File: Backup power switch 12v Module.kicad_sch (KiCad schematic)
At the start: 23 parts, among them J2 External, J5 Esternal, J9 PWR SELECTOR, K1 SRD-12VDC-SL-C, Q3 BSS138, U7 ESP32-C3 Pro Mini, U8 AMS1117-3.3

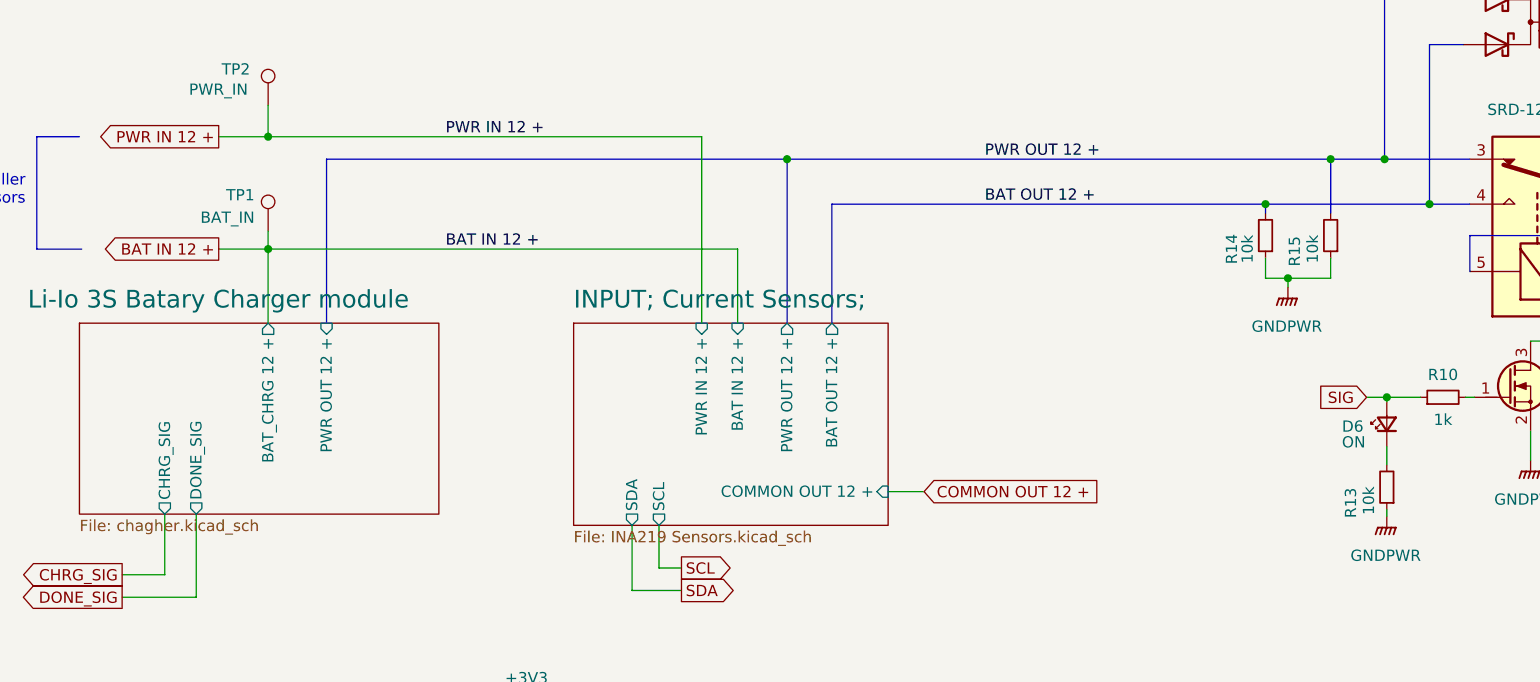
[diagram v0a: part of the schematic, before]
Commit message: Fix charger in/out nammes
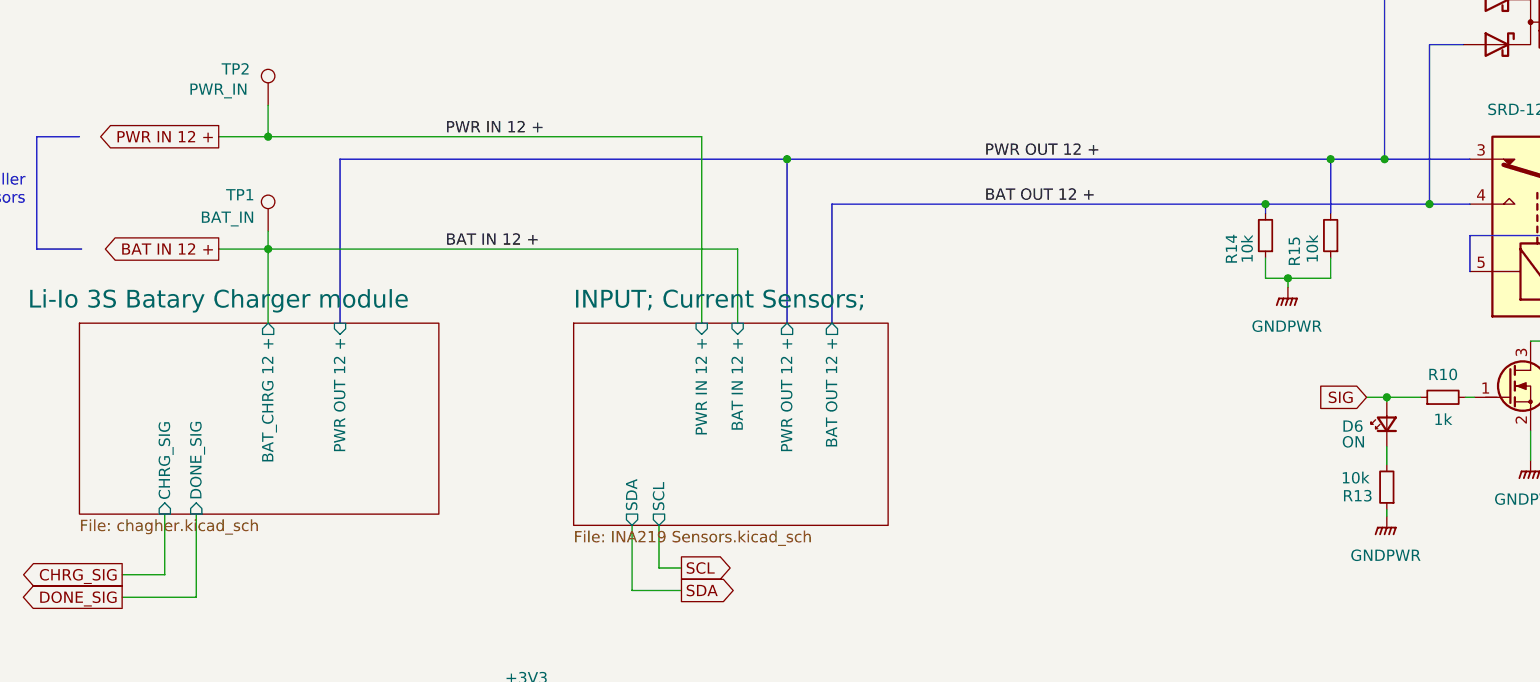
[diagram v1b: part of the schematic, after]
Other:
- sheet INPUT; Current Sensors; ports: added none; removed COMMON OUT 12 +
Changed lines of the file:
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@@
 	(bus
 		(pts
-			(xy 69.342 57.404) (xy 121.412 57.404)
+			(xy 70.866 57.404) (xy 121.412 57.404)
 		)
 		(stroke
@@
 	(wire
 		(pts
-			(xy 132.842 94.996) (xy 136.906 94.996)
-		)
-		(stroke
-			(width 0)
-			(type default)
-		)
-	)
-	(wire
-		(pts
 			(xy 213.868 77.978) (xy 214.376 77.978)
 		)
@@
 	(bus
 		(pts
-			(xy 69.342 57.404) (xy 69.342 75.946)
+			(xy 70.866 57.404) (xy 70.866 75.946)
 		)
 		(stroke
@@
 		)
 	)
-	(global_label "COMMON OUT 12 +"
-		(shape input)
-		(at 136.906 94.996 0)
-		(fields_autoplaced yes)
-		(effects
-			(font
-				(size 1.27 1.27)
-			)
-			(justify left)
-		)
-		(property "Intersheetrefs" "${INTERSHEET_REFS}"
-			(at 158.5783 94.996 0)
-			(show_name yes)
-			(effects
-				(font
-					(size 1.27 1.27)
-				)
-				(justify left)
-				(hide yes)
-			)
-		)
-	)
 	(global_label "BAT IN 12 +"
 		(shape input)
@@
 		(dnp no)
 		(property "Reference" "R13"
-			(at 185.166 96.266 90)
+			(at 185.928 95.504 0)
 			(effects
 				(font
@@
 		)
 		(property "Value" "10k"
-			(at 187.198 96.012 90)
+			(at 185.674 93.472 0)
 			(effects
 				(font
@@
 			)
 		)
-		(pin "COMMON OUT 12 +" input
-			(at 132.842 94.996 0)
-			(effects
-				(font
-					(size 1.27 1.27)
-				)
-				(justify right)
-			)
-		)
 		(pin "PWR IN 12 +" input
 			(at 111.76 75.946 90)
@@
 			)
 		)
-		(pin "BAT_CHRG 12 +" output
-			(at 62.738 75.946 90)
+		(pin "PWR OUT 12 +" input
+			(at 70.866 75.946 90)
 			(effects
 				(font
@@
 			)
 		)
-		(pin "PWR OUT 12 +" input
-			(at 69.342 75.946 90)
+		(pin "BAT_CHRG 12 +" output
+			(at 62.738 75.946 90)
 			(effects
 				(font
@@
 			)
 		)
-		(pin "CHRG_SIG" output
+		(pin "CHRG_SIG" input
 			(at 51.054 97.536 270)
 			(effects
@@
 			)
 		)
-		(pin "DONE_SIG" output
+		(pin "DONE_SIG" input
 			(at 54.61 97.536 270)
 			(effects

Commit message: Production
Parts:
- removed HS1: Heatsink, Heatsink:Heatsink_Stonecold_HS-S01_13.21x6.35mm, symbol Mechanical:Heatsink
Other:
- moved on the sheet: D6, J9, Q3, R10, R13

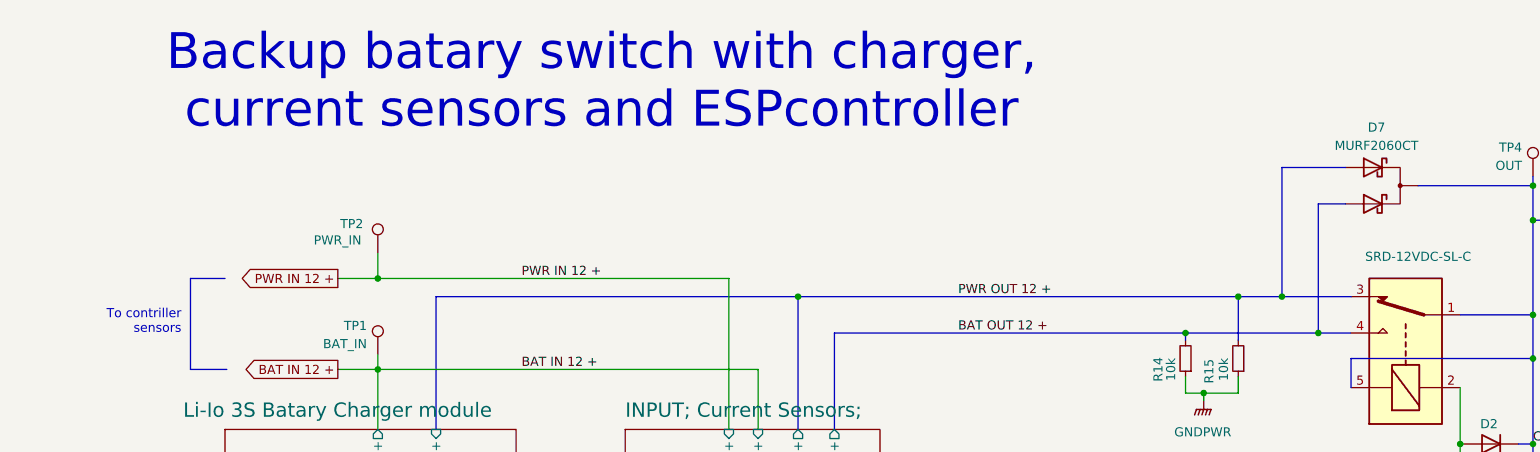
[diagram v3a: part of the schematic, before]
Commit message: Add more space aroung relay
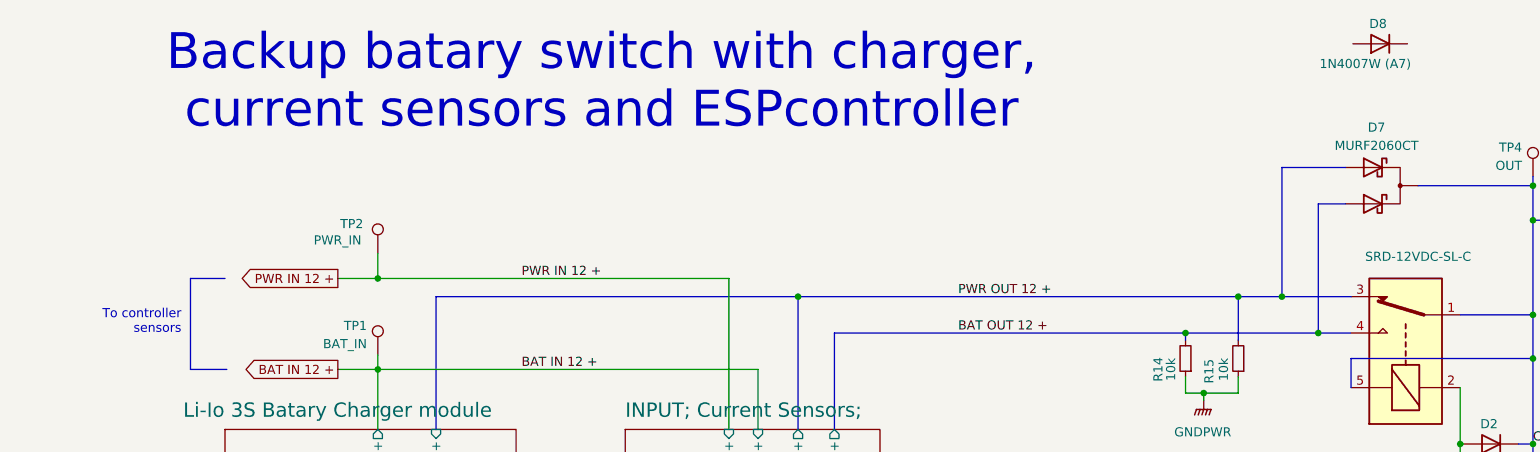
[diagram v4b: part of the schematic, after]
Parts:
- added D8: 1N4007W (A7), Diode_SMD:D_SMA, symbol Device:D
- C1: footprint Capacitor_SMD:C_1210_3225Metric_Pad1.33x2.70mm_HandSolder -> Capacitor_SMD:C_1206_3216Metric_Pad1.33x1.80mm_HandSolder
- D2: footprint Diode_SMD:D_SOD-123F -> Diode_SMD:D_SMA
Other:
- note added: "To controller sensors"
- note removed: "To contriller sensors"
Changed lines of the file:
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@@
 		)
 	)
-	(text "To contriller\nsensors\n\n"
+	(text "To controller\nsensors\n\n"
 		(exclude_from_sim no)
 		(at 35.306 61.976 0)
@@
 			)
 		)
-		(property "Footprint" "Diode_SMD:D_SOD-123F"
+		(property "Footprint" "Diode_SMD:D_SMA"
 			(at 218.186 77.978 0)
 			(hide yes)
@@
 			(at 218.186 77.978 0)
 			(hide yes)
+			(show_name no)
+			(do_not_autoplace no)
+			(effects
+				(font
+					(size 1.27 1.27)
+				)
+			)
+		)
+		(property "descr" ""
+			(at 218.186 77.978 0)
 			(show_name no)
 			(do_not_autoplace no)
@@
 			)
 		)
-		(property "Footprint" "Capacitor_SMD:C_1210_3225Metric_Pad1.33x2.70mm_HandSolder"
+		(property "Footprint" "Capacitor_SMD:C_1206_3216Metric_Pad1.33x1.80mm_HandSolder"
 			(at 215.392 143.256 0)
 			(hide yes)
@@
 					(unit 1)
 				)
+			)
+		)
+	)
+	(symbol
+		(lib_id "Device:D")
+		(at 202.692 22.098 180)
+		(unit 1)
+		(body_style 1)
+		(exclude_from_sim no)
+		(in_bom yes)
+		(on_board yes)
+		(in_pos_files yes)
+		(dnp no)
+		(property "Reference" "D8"
+			(at 201.168 19.304 0)
+			(show_name no)
+			(do_not_autoplace no)
+			(effects
+				(font
+					(size 1.27 1.27)
+				)
+				(justify right)
+			)
+		)
+		(property "Value" "1N4007W (A7)"
+			(at 207.01 24.892 0)
+			(show_name no)
+			(do_not_autoplace no)
+			(effects
+				(font
+					(size 1.27 1.27)
+				)
+				(justify left)
+			)
+		)
+		(property "Footprint" "Diode_SMD:D_SMA"
+			(at 202.692 22.098 0)
+			(hide yes)
+			(show_name no)
+			(do_not_autoplace no)
+			(effects
+				(font
+					(size 1.27 1.27)
+				)
+			)
+		)
+		(property "Datasheet" ""
+			(at 202.692 22.098 0)
+			(hide yes)
+			(show_name no)
+			(do_not_autoplace no)
+			(effects
+				(font
+					(size 1.27 1.27)
+				)
+			)
+		)
+		(property "Description" ""
+			(at 202.692 22.098 0)
+			(hide yes)
+			(show_name no)
+			(do_not_autoplace no)
+			(effects
+				(font
+					(size 1.27 1.27)
+				)
+			)
+		)
+		(property "descr" ""
+			(at 202.692 22.098 0)
+			(show_name no)
+			(do_not_autoplace no)
+			(effects
+				(font
+					(size 1.27 1.27)
+				)
+			)
+		)
+		(pin "1"
+		)
+		(pin "2"
+		)
+		(instances
+			(project "Backup power switch 12v Module"
+				(path "/7ca50d0f-f559-49b7-8c40-8a0dd824c105"
+					(reference "D8")
+					(unit 1)
+				)

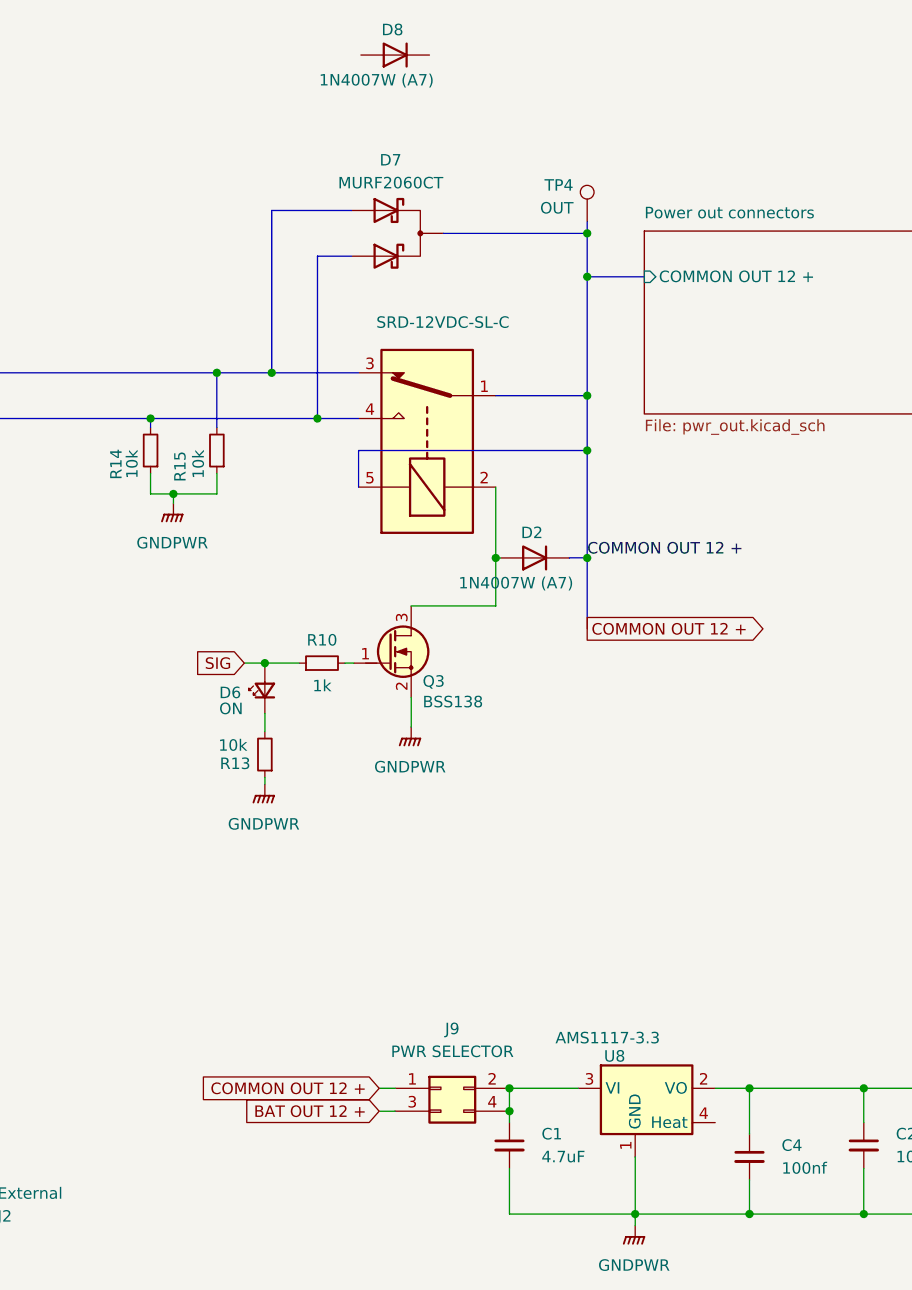
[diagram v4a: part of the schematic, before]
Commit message: Add holes for alt diodes. Prod. Docs
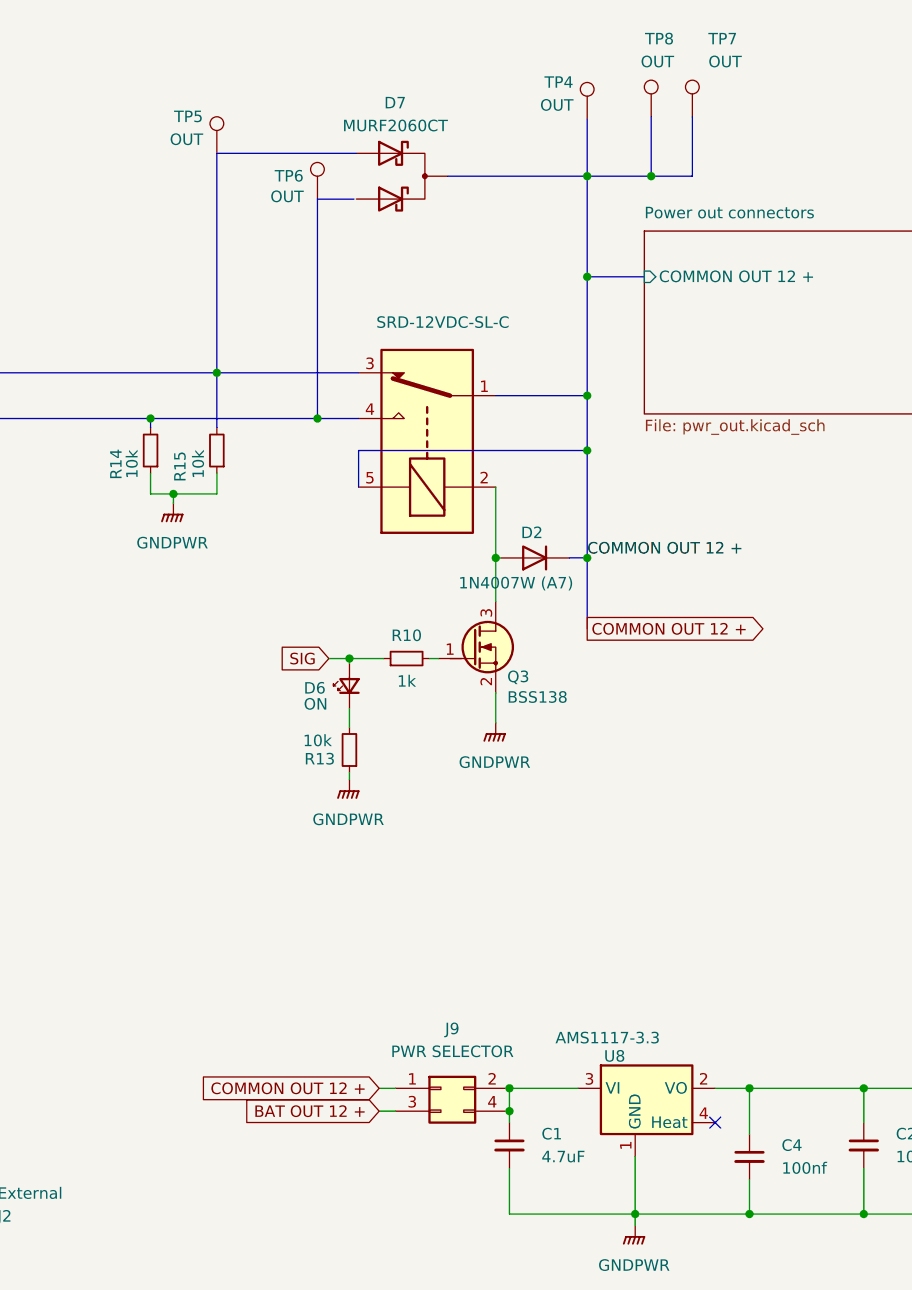
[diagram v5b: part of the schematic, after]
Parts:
- removed D8: 1N4007W (A7), Diode_SMD:D_SMA, symbol Device:D
- added TP5, TP6, TP7, TP8: OUT, TestPoint:TestPoint_Loop_D2.50mm_Drill1.85mm, symbol Connector:TestPoint
- U8: footprint Package_TO_SOT_SMD:SOT-223-3_TabPin2 -> Package_TO_SOT_SMD:SOT-223
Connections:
- no-connect marks 1 -> 2
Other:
- moved on the sheet: D6, D7, Q3, R10, R13, TP4
